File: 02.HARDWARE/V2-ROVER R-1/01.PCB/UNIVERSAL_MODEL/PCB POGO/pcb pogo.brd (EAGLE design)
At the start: 17 x 17 mm, 0 parts

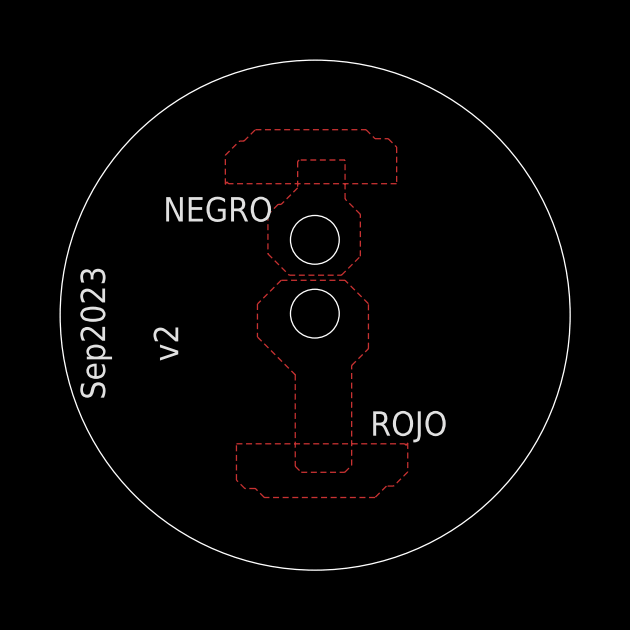
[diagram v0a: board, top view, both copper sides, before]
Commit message: Modificacion v3 Pogo pin universal
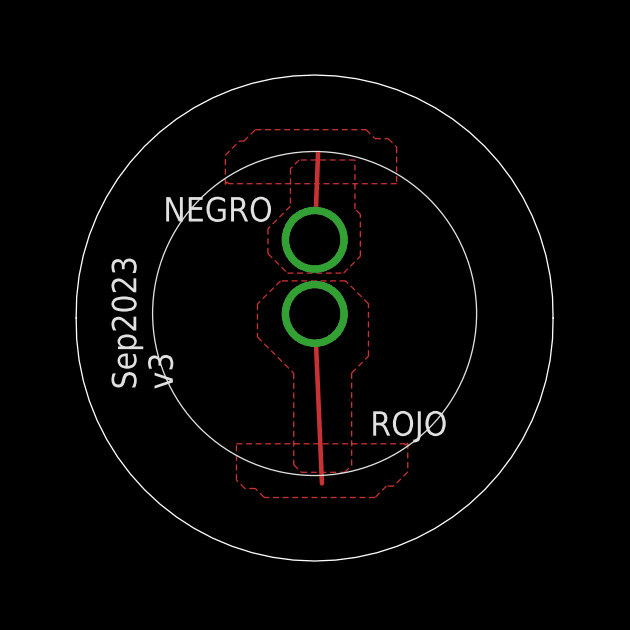
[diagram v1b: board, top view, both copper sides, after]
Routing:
- net POS+: track 0.00 -> 5.66 mm, vias 0 -> 1
- net NEG-: track 0.00 -> 2.90 mm, vias 0 -> 1
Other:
- board size 17 x 17 mm -> 15.9 x 16.2 mm
- board text added: "Sep2023 v3"
- board text removed: "Sep2023 v2"
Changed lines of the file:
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@@
 <board>
 <plain>
-<circle x="7.073309375" y="8.648309375" radius="0.8125" width="0.01" layer="20"/>
-<circle x="7.073309375" y="6.18831875" radius="6.5" width="0.01" layer="51"/>
-<circle x="7.073309375" y="6.18831875" radius="0.8125" width="0.01" layer="20"/>
 <polygon width="0.01" layer="29">
-<vertex x="7.28" y="10.59"/>
-<vertex x="6.72" y="10.59"/>
-<vertex x="5.54" y="9.41"/>
-<vertex x="5.54" y="8.27"/>
-<vertex x="6.24" y="7.57"/>
-<vertex x="6.24" y="7.54"/>
-<vertex x="6.25" y="7.55"/>
-<vertex x="7.95" y="7.55"/>
-<vertex x="8.55" y="8.15"/>
-<vertex x="8.55" y="9.32"/>
+<vertex x="8.08" y="10"/>
+<vertex x="6.47" y="10"/>
+<vertex x="5.54" y="9.07"/>
+<vertex x="5.54" y="8.17"/>
+<vertex x="6.17" y="7.54"/>
+<vertex x="8.04" y="7.54"/>
+<vertex x="8.6" y="8.1"/>
+<vertex x="8.6" y="9.48"/>
 </polygon>
 <polygon width="0.01" layer="29">
@@
 </polygon>
 <polygon width="0.01" layer="29">
-<vertex x="6.04" y="7.13"/>
-<vertex x="5.44" y="6.53"/>
-<vertex x="5.44" y="4.88"/>
-<vertex x="6.4" y="3.92"/>
-<vertex x="7.88" y="3.92"/>
-<vertex x="8.68" y="4.72"/>
-<vertex x="8.68" y="6.37"/>
-<vertex x="7.85" y="7.2"/>
-<vertex x="6.1" y="7.2"/>
-<vertex x="6.03" y="7.13"/>
-<vertex x="6.04" y="7.12"/>
+<vertex x="5.92" y="7.28"/>
+<vertex x="5.14" y="6.5"/>
+<vertex x="5.14" y="5.44"/>
+<vertex x="6.37" y="4.21"/>
+<vertex x="8.29" y="4.21"/>
+<vertex x="8.86" y="4.78"/>
+<vertex x="8.86" y="6.54"/>
+<vertex x="8.12" y="7.28"/>
 </polygon>
 <polygon width="0.01" layer="29">
-<vertex x="6.55" y="10.75"/>
-<vertex x="6.55" y="10.14"/>
-<vertex x="6.77" y="9.92"/>
-<vertex x="6.8" y="9.95"/>
-<vertex x="8.04" y="9.95"/>
-<vertex x="8.04" y="11.33"/>
+<vertex x="6.28" y="10.75"/>
+<vertex x="6.28" y="9.79"/>
+<vertex x="6.46" y="9.61"/>
+<vertex x="6.57" y="9.72"/>
+<vertex x="8.38" y="9.72"/>
+<vertex x="8.38" y="11.67"/>
 <vertex x="7.46" y="10.75"/>
 </polygon>
 <text x="8.92" y="2.12" size="0.8128" layer="25" font="vector">ROJO</text>
 <text x="2.02" y="9.26" size="0.8128" layer="25" font="vector">NEGRO</text>
-<text x="2.52" y="3.32" size="0.8128" layer="25" font="vector" rot="R90">Sep2023
-    v2</text>
-<circle x="7.083309375" y="6.13831875" radius="8.5" width="0.01" layer="20"/>
+<text x="2.34" y="3.66" size="0.8128" layer="25" font="vector" rot="R90">Sep2023
+v3</text>
 <polygon width="0.1524" layer="29">
 <vertex x="10.17" y="1.88"/>
@@
 <vertex x="4.1" y="10.6"/>
 </polygon>
+<wire x1="15.01358125" y1="6.0425" x2="-0.88358125" y2="6.0425" width="0.001" layer="20" curve="182.162234"/>
+<wire x1="-0.88358125" y1="6.0425" x2="15.01358125" y2="6.0425" width="0.001" layer="20" curve="182.162234"/>
+<circle x="7.065" y="6.1925" radius="5.4" width="0.001" layer="21"/>
 </plain>
 <attributes>
@@
 <param name="mdViaViaSameLayer" value="6mil"/>
 <param name="mnLayersViaInSmd" value="2"/>
-<param name="mdCopperDimension" value="0mil"/>
-<param name="mdDrill" value="0mil"/>
+<param name="mdCopperDimension" value="1mil"/>
+<param name="mdDrill" value="1mil"/>
 <param name="mdSmdStop" value="0mil"/>
 <param name="msWidth" value="6mil"/>
@@
 <param name="msMicroVia" value="9.99mm"/>
 <param name="msBlindViaRatio" value="0.5"/>
-<param name="rvPadTop" value="0.25"/>
-<param name="rvPadInner" value="0.25"/>
-<param name="rvPadBottom" value="0.25"/>
-<param name="rvViaOuter" value="0.25"/>
-<param name="rvViaInner" value="0.25"/>
-<param name="rvMicroViaOuter" value="0.25"/>
-<param name="rvMicroViaInner" value="0.25"/>
-<param name="rlMinPadTop" value="10mil"/>
+<param name="rvPadTop" value="0.15"/>
+<param name="rvPadInner" value="0.15"/>
+<param name="rvPadBottom" value="0.15"/>
+<param name="rvViaOuter" value="0.15"/>
+<param name="rvViaInner" value="0.15"/>
+<param name="rvMicroViaOuter" value="0.15"/>
+<param name="rvMicroViaInner" value="0.15"/>
+<param name="rlMinPadTop" value="1mil"/>
 <param name="rlMaxPadTop" value="20mil"/>
-<param name="rlMinPadInner" value="10mil"/>
+<param name="rlMinPadInner" value="1mil"/>
 <param name="rlMaxPadInner" value="20mil"/>
-<param name="rlMinPadBottom" value="10mil"/>
+<param name="rlMinPadBottom" value="1mil"/>
 <param name="rlMaxPadBottom" value="20mil"/>
-<param name="rlMinViaOuter" value="8mil"/>
+<param name="rlMinViaOuter" value="1mil"/>
 <param name="rlMaxViaOuter" value="20mil"/>
-<param name="rlMinViaInner" value="8mil"/>
+<param name="rlMinViaInner" value="1mil"/>
 <param name="rlMaxViaInner" value="20mil"/>
-<param name="rlMinMicroViaOuter" value="4mil"/>
+<param name="rlMinMicroViaOuter" value="1mil"/>
 <param name="rlMaxMicroViaOuter" value="20mil"/>
-<param name="rlMinMicroViaInner" value="4mil"/>
+<param name="rlMinMicroViaInner" value="1mil"/>
 <param name="rlMaxMicroViaInner" value="20mil"/>
 <param name="psTop" value="-1"/>
@@
 <signal name="NEG-">
 <polygon width="0.01" layer="1" isolate="0.254">
-<vertex x="5.85" y="9.83"/>
-<vertex x="5.51" y="9.49"/>
-<vertex x="5.51" y="8.18"/>
-<vertex x="6.22" y="7.47"/>
-<vertex x="7.96" y="7.47"/>
+<vertex x="6.26" y="9.77"/>
+<vertex x="5.51" y="9.02"/>
+<vertex x="5.51" y="8.19"/>
+<vertex x="6.16" y="7.54"/>
+<vertex x="8.03" y="7.54"/>
 <vertex x="8.59" y="8.1"/>
 <vertex x="8.59" y="9.5"/>
-<vertex x="8.08" y="10.01"/>
-<vertex x="8.08" y="11.31"/>
+<vertex x="8.41" y="9.68"/>
+<vertex x="8.41" y="11.31"/>
 <vertex x="6.55" y="11.31"/>
-<vertex x="6.5" y="11.26"/>
-<vertex x="6.5" y="10.38"/>
-<vertex x="5.95" y="9.83"/>
+<vertex x="6.26" y="11.02"/>
 </polygon>
 <polygon width="0.1524" layer="1">
@@
 <vertex x="4.14" y="10.58"/>
 </polygon>
+<via x="7.07" y="8.65" extent="1-16" drill="1.7"/>
+<wire x1="7.07" y1="8.65" x2="7.18" y2="11.55" width="0.1524" layer="1"/>
 </signal>
 <signal name="POS+">
 <polygon width="0.01" layer="1" isolate="0.254">
-<vertex x="8.08" y="7.3"/>
-<vertex x="5.95" y="7.3"/>
+<vertex x="8.1" y="7.28"/>
+<vertex x="5.93" y="7.28"/>
 <vertex x="5.16" y="6.51"/>
 <vertex x="5.16" y="5.41"/>
-<vertex x="6.41" y="4.16"/>
-<vertex x="6.42" y="4.16"/>
-<vertex x="6.42" y="1.1"/>
+<vertex x="6.37" y="4.2"/>
+<vertex x="6.37" y="1.15"/>
 <vertex x="6.62" y="0.9"/>
 <vertex x="8.07" y="0.9"/>
 <vertex x="8.3" y="1.13"/>
-<vertex x="8.3" y="4.46"/>
-<vertex x="8.86" y="5.02"/>
+<vertex x="8.3" y="4.21"/>
+<vertex x="8.86" y="4.77"/>
 <vertex x="8.86" y="6.52"/>
 </polygon>
@@
 <vertex x="10.12" y="1.8"/>
 </polygon>
+<via x="7.07" y="6.18" extent="1-16" drill="1.7"/>
+<wire x1="7.07" y1="6.18" x2="7.31" y2="0.53" width="0.1524" layer="1"/>
 </signal>
 </signals>

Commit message: Ajustes PCBs
Cambio en el pcb de cheyenne para que entre en el adapatador de la universal.
Cambio en el pcb del pogo para que se ajuste mejor a los adaptadores de la universal
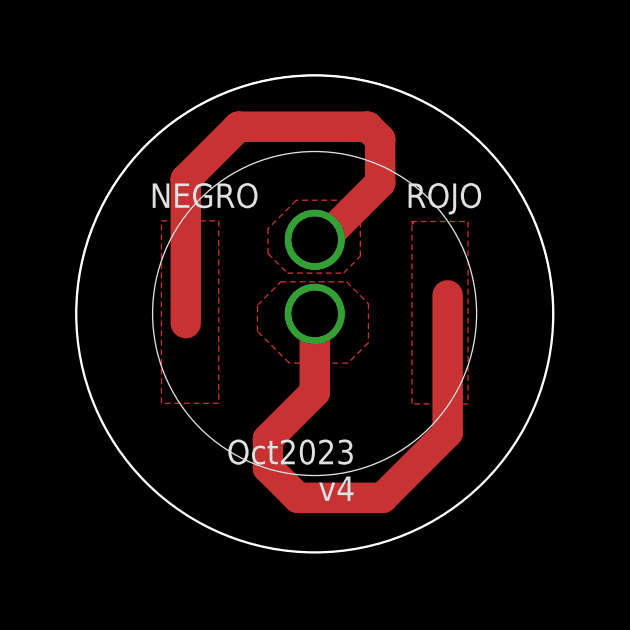
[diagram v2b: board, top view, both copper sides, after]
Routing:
- net NEG-: track 2.90 -> 16.7 mm
- net POS+: track 5.66 -> 17.7 mm
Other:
- board size 15.9 x 16.2 mm -> 15.9 x 15.9 mm
- board text added: "Oct2023 v4"
- board text added: "ROVER R-1"
- board text removed: "Sep2023 v3"

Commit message: Modificaciones para solucionar issue #75 (WIP)
Todavia pendiente de hacer mas cambios
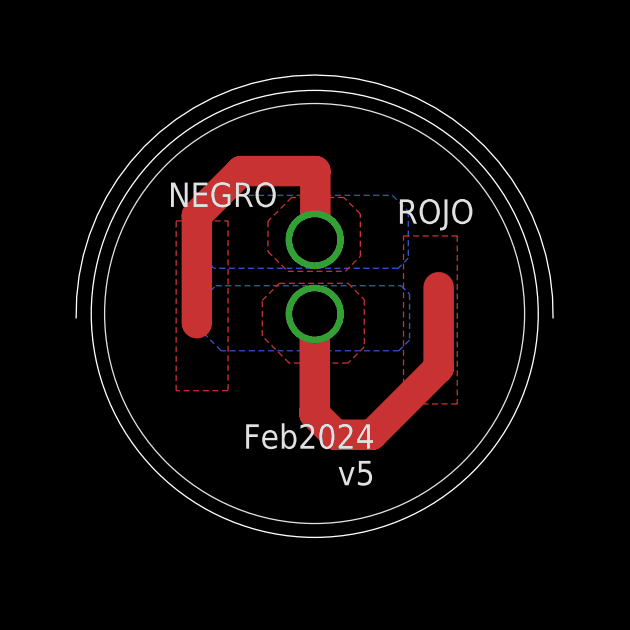
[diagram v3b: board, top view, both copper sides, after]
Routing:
- net POS+: track 17.7 -> 11.4 mm
- net NEG-: track 16.7 -> 10.5 mm
- added copper zone on layer 16, net NEG-
- added copper zone on layer 16, net POS+
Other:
- board size 15.9 x 15.9 mm -> 15.9 x 15.4 mm
- board text added: "Feb2024 v5"
- board text removed: "Oct2023 v4"
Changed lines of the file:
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@@
 <grid distance="0.01" unitdist="mm" unit="mm" style="lines" multiple="1" display="no" altdistance="5" altunitdist="mil" altunit="mm"/>
 <layers>
-<layer number="1" name="Top" color="4" fill="1" visible="yes" active="yes"/>
+<layer number="1" name="Top" color="4" fill="1" visible="no" active="yes"/>
 <layer number="2" name="Route2" color="16" fill="1" visible="no" active="no"/>
 <layer number="15" name="Route15" color="23" fill="1" visible="no" active="no"/>
@@
 <vertex x="8.38" y="9.72"/>
 </polygon>
-<text x="10.1" y="9.715" size="0.8128" layer="25" font="vector">ROJO</text>
-<text x="1.57" y="9.715" size="0.8128" layer="25" font="vector">NEGRO</text>
-<text x="8.42" y="1.98" size="0.8128" layer="25" font="vector" rot="R180">Oct2023
-v4</text>
+<text x="9.81" y="9.185" size="0.8128" layer="25" font="vector">ROJO</text>
+<text x="2.18" y="9.745" size="0.8128" layer="25" font="vector">NEGRO</text>
+<text x="9.07" y="2.5" size="0.8128" layer="25" font="vector" rot="R180">Feb2024
+v5</text>
 <polygon width="0.1524" layer="29">
 <vertex x="10.34" y="9.253334375"/>
@@
 </polygon>
 <wire x1="15.01358125" y1="6.0425" x2="-0.88358125" y2="6.0425" width="0.001" layer="20" curve="182.162234"/>
-<circle x="7.065" y="6.1925" radius="5.4" width="0.001" layer="21"/>
-<circle x="7.07" y="6.18" radius="7.95" width="0.0762" layer="20"/>
+<circle x="7.065" y="6.1925" radius="7" width="0.001" layer="21"/>
+<circle x="7.07" y="6.18" radius="7.45" width="0.00761875" layer="20"/>
 <polygon width="0.1524" layer="29">
 <vertex x="3.916" y="3.146665625"/>
@@
 <signal name="NEG-">
 <polygon width="0.01" layer="1" isolate="0.254">
-<vertex x="6.46" y="9.97"/>
-<vertex x="5.51" y="9.02"/>
-<vertex x="5.51" y="8.19"/>
-<vertex x="6.16" y="7.54"/>
-<vertex x="8.03" y="7.54"/>
+<vertex x="6.3" y="10.06"/>
+<vertex x="5.51" y="9.27"/>
+<vertex x="5.51" y="8.26"/>
+<vertex x="6.17" y="7.6"/>
+<vertex x="8.09" y="7.6"/>
 <vertex x="8.59" y="8.1"/>
 <vertex x="8.59" y="9.51"/>
-<vertex x="8.13" y="9.97"/>
-</polygon>
-<via x="7.07" y="8.65" extent="1-16" drill="1.55"/>
-<wire x1="2.77" y1="10.66" x2="2.77" y2="5.87" width="1.016" layer="1"/>
-<wire x1="9.25" y1="10.55" x2="7.25" y2="8.55" width="1.016" layer="1"/>
-<wire x1="7.25" y1="8.55" x2="7.17" y2="8.55" width="1.016" layer="1"/>
-<wire x1="7.07" y1="8.65" x2="7.17" y2="8.55" width="1.016" layer="1"/>
-<wire x1="9.25" y1="12" x2="9.25" y2="10.55" width="1.016" layer="1"/>
-<wire x1="9.25" y1="12" x2="8.83" y2="12.42" width="1.016" layer="1"/>
-<wire x1="8.83" y1="12.42" x2="4.53" y2="12.42" width="1.016" layer="1"/>
-<wire x1="4.53" y1="12.42" x2="2.77" y2="10.66" width="1.016" layer="1"/>
+<vertex x="8.04" y="10.06"/>
+</polygon>
+<via x="7.07" y="8.65" extent="1-16" drill="1.5"/>
+<wire x1="3.14" y1="9.46" x2="3.14" y2="5.87" width="1.016" layer="1"/>
+<wire x1="7.09" y1="10.94" x2="7.09" y2="8.67" width="1.016" layer="1"/>
+<wire x1="7.07" y1="8.65" x2="7.09" y2="8.67" width="1.016" layer="1"/>
+<wire x1="7.09" y1="10.94" x2="4.62" y2="10.94" width="1.016" layer="1"/>
+<wire x1="4.62" y1="10.94" x2="3.14" y2="9.46" width="1.016" layer="1"/>
 <polygon width="0.1524" layer="1">
-<vertex x="3.87" y="3.2"/>
-<vertex x="1.96" y="3.2"/>
-<vertex x="1.96" y="9.28"/>
-<vertex x="3.87" y="9.28"/>
+<vertex x="4.18" y="3.62"/>
+<vertex x="2.45" y="3.62"/>
+<vertex x="2.45" y="9.28"/>
+<vertex x="4.18" y="9.28"/>
+</polygon>
+<polygon width="0.0762" layer="16">
+<vertex x="3.9" y="10.13"/>
+<vertex x="9.66" y="10.13"/>
+<vertex x="10.19" y="9.6"/>
+<vertex x="10.19" y="8.04"/>
+<vertex x="9.85" y="7.7"/>
+<vertex x="3.71" y="7.7"/>
+<vertex x="3.46" y="7.95"/>
+<vertex x="3.46" y="9.69"/>
 </polygon>
 </signal>
 <signal name="POS+">
 <polygon width="0.1524" layer="1">
-<vertex x="10.28" y="9.26"/>
-<vertex x="12.18" y="9.26"/>
-<vertex x="12.18" y="3.18"/>
-<vertex x="10.31" y="3.18"/>
-<vertex x="10.31" y="9.16"/>
-<vertex x="10.36" y="9.21"/>
-</polygon>
-<via x="7.07" y="6.18" extent="1-16" drill="1.55"/>
-<polygon width="0.1524" layer="1">
-<vertex x="5.92" y="7.25"/>
-<vertex x="8.13" y="7.25"/>
-<vertex x="8.86" y="6.52"/>
-<vertex x="8.86" y="5.22"/>
+<vertex x="10.03" y="8.78"/>
+<vertex x="11.82" y="8.78"/>
+<vertex x="11.82" y="3.18"/>
+<vertex x="10.03" y="3.18"/>
+</polygon>
+<via x="7.07" y="6.18" extent="1-16" drill="1.5"/>
+<polygon width="0.0762" layer="1">
+<vertex x="5.89" y="7.2"/>
+<vertex x="8.18" y="7.2"/>
+<vertex x="8.72" y="6.66"/>
+<vertex x="8.72" y="5.08"/>
 <vertex x="8.18" y="4.54"/>
 <vertex x="6.22" y="4.54"/>
-<vertex x="5.16" y="5.6"/>
-<vertex x="5.16" y="6.47"/>
-<vertex x="5.89" y="7.2"/>
-<vertex x="5.91" y="7.2"/>
-</polygon>
-<wire x1="7.07" y1="6.18" x2="7.07" y2="3.57" width="1.016" layer="1"/>
-<wire x1="7.07" y1="3.57" x2="5.51" y2="2.01" width="1.016" layer="1"/>
-<wire x1="5.51" y1="2.01" x2="5.51" y2="1.04958125" width="1.016" layer="1"/>
-<wire x1="6.50958125" y1="0.05" x2="9.33" y2="0.05" width="1.016" layer="1"/>
-<wire x1="9.33" y1="0.05" x2="11.5" y2="2.22" width="1.016" layer="1"/>
-<wire x1="11.5" y1="2.22" x2="11.5" y2="6.8" width="1.016" layer="1"/>
-<wire x1="5.51" y1="1.04958125" x2="6.50958125" y2="0.05" width="1.016" layer="1"/>
+<vertex x="5.32" y="5.44"/>
+<vertex x="5.32" y="6.63"/>
+</polygon>
+<wire x1="7.07" y1="6.18" x2="7.07" y2="2.91" width="1.016" layer="1"/>
+<wire x1="7.07" y1="2.91" x2="7.06" y2="2.9" width="1.016" layer="1"/>
+<wire x1="7.06" y1="2.9" x2="7.06" y2="2.84958125" width="1.016" layer="1"/>
+<wire x1="7.75958125" y1="2.15" x2="8.97" y2="2.15" width="1.016" layer="1"/>
+<wire x1="8.97" y1="2.15" x2="11.2" y2="4.38" width="1.016" layer="1"/>
+<wire x1="11.2" y1="4.38" x2="11.2" y2="7.07" width="1.016" layer="1"/>
+<wire x1="7.06" y1="2.84958125" x2="7.75958125" y2="2.15" width="1.016" layer="1"/>
+<polygon width="0.0762" layer="16">
+<vertex x="3.77" y="7.12"/>
+<vertex x="9.95" y="7.12"/>
+<vertex x="10.23" y="6.84"/>
+<vertex x="10.23" y="5.31"/>
+<vertex x="9.87" y="4.95"/>
+<vertex x="3.95" y="4.95"/>
+<vertex x="3.36" y="5.54"/>
+<vertex x="3.36" y="6.71"/>
+</polygon>
 </signal>
 </signals>
